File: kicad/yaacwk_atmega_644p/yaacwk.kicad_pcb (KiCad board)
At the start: 2 copper layers, 110 x 78 mm, 61 parts, among them IC1 ATMEGA644P-P, IC2 TLP627-2, J1 EXT_PWR, J2 AUDIO_IN, J3 TX_PTT, J4 TX_KEY, J5 PADDLES, J6 TTL_SERIAL, SW1 SW_PUSH, SW2 SW_PUSH, SW3 SW_PUSH, SW4 SW_PUSH, SW5 SW_PUSH, SW6 SW_PUSH, U1 LM7805, Y1 Crystal 16 Mhz

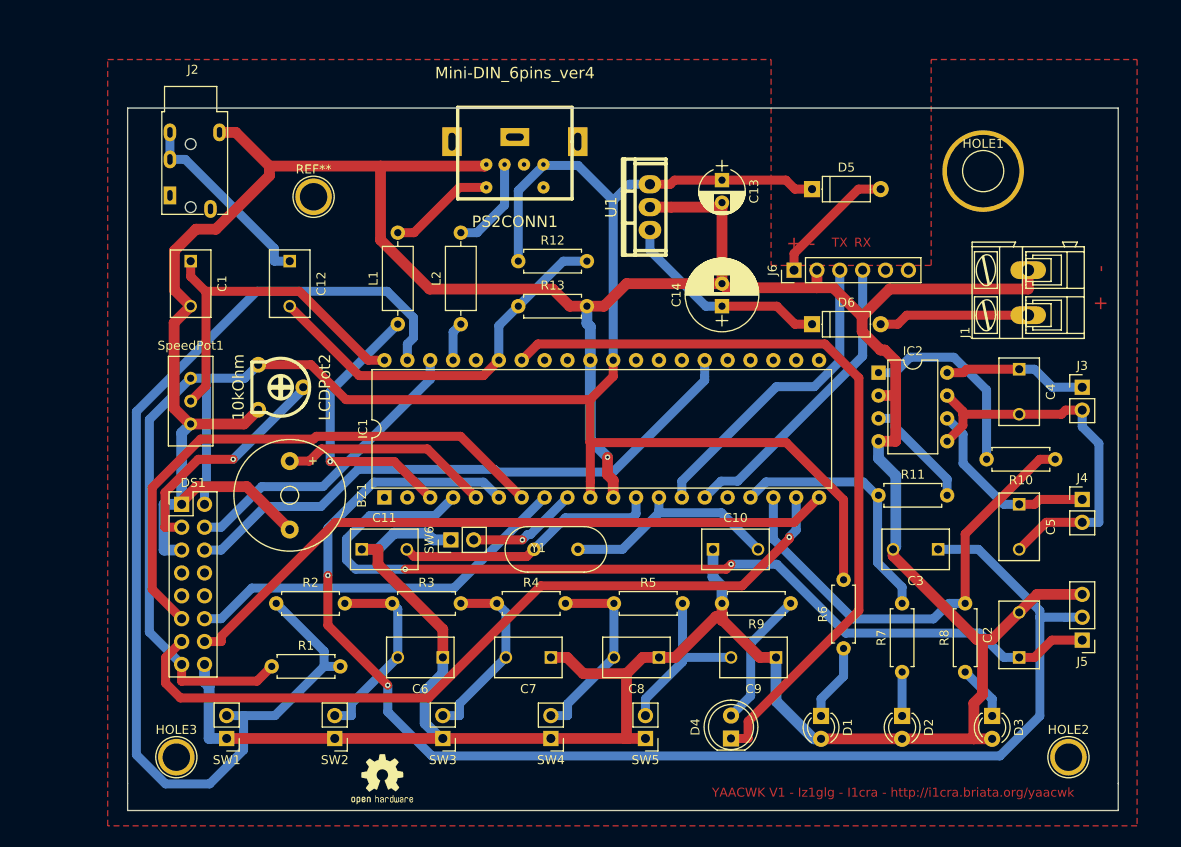
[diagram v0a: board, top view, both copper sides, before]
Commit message: yaacwk pcb v1.1_RC updated eechema
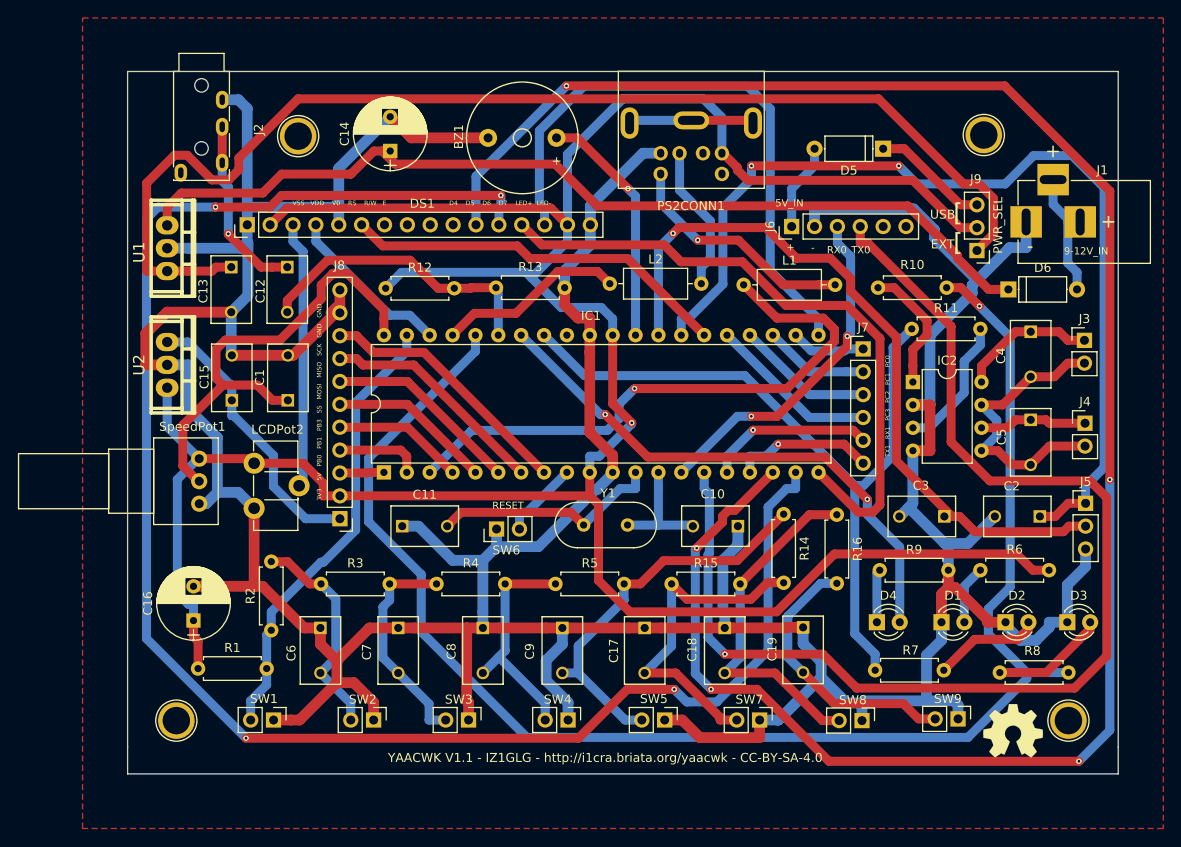
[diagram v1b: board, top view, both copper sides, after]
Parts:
- removed G***: LOGO, OPENHARDWARE:OSHWLOGO0.3IN
- added C15: 220nF, Capacitors_ThroughHole:C_Disc_D7.5_P5, F.Cu at (111.6, 92.5)
- added C16: 330uF, Capacitors_THT:CP_Radial_D8.0mm_P3.80mm, F.Cu at (107.3, 116.9)
- added C17: 100nF, Capacitors_ThroughHole:C_Disc_D7.5_P5, F.Cu at (157.4, 117.7)
- added C18: 100nF, Capacitors_ThroughHole:C_Disc_D7.5_P5, F.Cu at (166.3, 117.7)
- added C19: 100nF, Capacitors_ThroughHole:C_Disc_D7.5_P5, F.Cu at (175.0, 117.7)
- added J7: HEADER_6, Pin_Headers:Pin_Header_Straight_1x06_Pitch2.54mm, F.Cu at (181.7, 86.7)
- added J8: HEADER_11, Pin_Headers:Pin_Header_Straight_1x11_Pitch2.54mm, F.Cu at (123.6, 105.6)
- added J9: PWR_SEL, Pin_Headers:Pin_Header_Straight_1x03_Pitch2.54mm, F.Cu at (194.3, 75.8)
- added R14: 1kOhm, Resistors_THT:R_Axial_DIN0207_L6.3mm_D2.5mm_P7.62mm_Horizontal, F.Cu at (172.8, 105.1)
- added R15: 1kOhm, Resistors_THT:R_Axial_DIN0207_L6.3mm_D2.5mm_P7.62mm_Horizontal, F.Cu at (160.4, 112.8)
- added R16: 1kOhm, Resistors_THT:R_Axial_DIN0207_L6.3mm_D2.5mm_P7.62mm_Horizontal, F.Cu at (178.8, 105.2)
- added REF***: OSHW-Symbol_6.7x6mm_SilkScreen, Symbols:OSHW-Symbol_6.7x6mm_SilkScreen, F.Cu at (198.3, 129.2)
- added SW7: SW_PUSH, Pin_Headers:Pin_Header_Straight_1x02_Pitch2.54mm, F.Cu at (170.2, 128.0)
- added SW8: SW_PUSH, Pin_Headers:Pin_Header_Straight_1x02_Pitch2.54mm, F.Cu at (181.5, 128.0)
- added SW9: SW_PUSH, Pin_Headers:Pin_Header_Straight_1x02_Pitch2.54mm, F.Cu at (192.2, 127.8)
- added U2: LM2937, mojes-kicad-footprints:78XX, F.Cu at (104.4, 88.5)
- C13: value 50mF -> 220nF; footprint Capacitors_THT:CP_Radial_D5.0mm_P2.50mm -> Capacitors_ThroughHole:C_Disc_D7.5_P5
- C14: value 350mF -> 330uF; footprint Capacitors_THT:CP_Radial_D8.0mm_P2.50mm -> Capacitors_THT:CP_Radial_D8.0mm_P3.80mm
- D4: footprint LEDs:LED_D5.0mm -> LEDs:LED_D3.0mm
- DS1: footprint Pin_Headers:Pin_Header_Straight_2x08_Pitch2.54mm -> Pin_Headers:Pin_Header_Straight_1x16_Pitch2.54mm
- HOLE1: footprint Connectors:1pin -> Connect:1pin
- J1: footprint Connect:AK300-2 -> Connectors:BARREL_JACK
- J2: footprint custom_kicad_footprints:PJ320E_3.5mm_4_conductors_audio_plug -> PJ320A:PJ320A_3.5mm_4_conductors_audio_plug
- LCDPot2: footprint w_pth_resistors:trimmer_piher_pt6xv -> Potentiometers:Potentiometer_Trimmer_ACP_CA9h5_Vertical_Px5.0mm_Py5.0mm
- PS2CONN1: footprint mini_din6:Mini_din6 -> mini_din6New:Mini_din6
- R6, R7, R8: value 1kOhm -> 470 Ohm
- SpeedPot1: footprint Potentiometers:Potentiometer_Trimmer_Suntan_TSR-3386C_Vertical -> Potentiometers:Potentiometer_Alps_RK097_Single_Vertical
- Y1: value Crystal 16 Mhz -> Crystal 16 MHz
- moved C13 55.3 mm to (111.5, 77.7)
- moved U1 53.8 mm to (104.4, 75.6), turned to 270 degrees
- moved BZ1 47.4 mm to (143.8, 63.3), turned to 180 degrees
- moved C14 40.7 mm to (129.2, 64.8)
- moved L1 38.6 mm to (168.4, 79.6), turned to 0 degrees
- moved DS1 31.9 mm to (113.3, 73.0), turned to 90 degrees
- moved C9 24.0 mm to (148.3, 117.7), turned to 270 degrees
- moved R10 22.5 mm to (190.9, 79.9)
- moved D6 22.1 mm to (197.8, 80.1)
- moved D4 20.7 mm to (183.2, 117.1), turned to 0 degrees
- moved C8 19.8 mm to (139.4, 117.7), turned to 270 degrees
- moved C1 18.9 mm to (117.8, 92.5), turned to 90 degrees
- moved R11 18.8 mm to (187.1, 84.5)
- moved PS2CONN1 18.3 mm to (161.3, 64.5)
- moved R6 17.5 mm to (194.7, 111.3), turned to 0 degrees
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- renumbered REF** to HOLE0
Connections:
- D1 pad 1: Net-(D1-Pad1) -> GND
- D1 pad 2: GND -> Net-(D1-Pad2)
- D2 pad 1: Net-(D2-Pad1) -> GND
- D2 pad 2: GND -> Net-(D2-Pad2)
- D3 pad 1: Net-(D3-Pad1) -> GND
- D3 pad 2: GND -> Net-(D3-Pad2)
- D5 pad 1: Net-(C13-Pad1) -> Net-(D5-Pad1)
- DS1 pad 15: Net-(C13-Pad1) -> Net-(C16-Pad1)
- DS1 pad 2: Net-(C13-Pad1) -> Net-(C16-Pad1)
- IC1 pad 10: Net-(C13-Pad1) -> Net-(C16-Pad1)
- IC1 pad 18: Net-(IC1-Pad18) -> Net-(DS1-Pad11)
- IC1 pad 19: Net-(DS1-Pad13) -> Net-(DS1-Pad12)
- IC1 pad 20: Net-(DS1-Pad14) -> Net-(DS1-Pad13)
- IC1 pad 21: Net-(IC1-Pad21) -> Net-(DS1-Pad14)
- IC1 pad 27: Net-(IC1-Pad27) -> Net-(C2-Pad1)
- IC1 pad 28: Net-(IC1-Pad28) -> Net-(C3-Pad1)
- IC1 pad 29: Net-(IC1-Pad29) -> Net-(BZ1-Pad1)
- IC1 pad 30: Net-(C13-Pad1) -> Net-(C16-Pad1)
- IC1 pad 34: Net-(D4-Pad1) -> Net-(D4-Pad2)
- IC1 pad 4: Net-(C2-Pad1) -> Net-(IC1-Pad4)
- IC1 pad 5: Net-(BZ1-Pad1) -> Net-(IC1-Pad5)
- IC1 pad 6: Net-(C3-Pad1) -> Net-(IC1-Pad6)
- IC1 pad 7: Net-(DS1-Pad11) -> Net-(IC1-Pad7)
- IC1 pad 8: Net-(DS1-Pad12) -> Net-(IC1-Pad8)
- J1 pad 1: Net-(D6-Pad2) -> GND
- J1 pad 2: GND -> Net-(D6-Pad2)
- J2 pad 2: Net-(C12-Pad1) -> GND
- J2 pad 4: Net-(J2-Pad4) -> Net-(C12-Pad1)
- J2 pad 5: GND -> Net-(J2-Pad5)
- LCDPot2 pad 1: Net-(C13-Pad1) -> Net-(C16-Pad1)
- PS2CONN1 pad 4: Net-(C13-Pad1) -> Net-(C16-Pad1)
- R1 pad 1: Net-(C13-Pad1) -> Net-(C16-Pad1)
- R10 pad 1: Net-(IC1-Pad18) -> Net-(IC1-Pad36)
- R11 pad 1: Net-(IC1-Pad17) -> Net-(IC1-Pad33)
- R12 pad 1: Net-(C13-Pad1) -> Net-(C16-Pad1)
- R6 pad 1: Net-(D1-Pad1) -> Net-(D1-Pad2)
- R6 pad 2: Net-(C13-Pad1) -> Net-(C16-Pad1)
- R7 pad 1: Net-(D2-Pad1) -> Net-(D2-Pad2)
- R7 pad 2: Net-(IC1-Pad17) -> Net-(IC1-Pad33)
- R8 pad 1: Net-(D3-Pad1) -> Net-(D3-Pad2)
- R8 pad 2: Net-(IC1-Pad18) -> Net-(IC1-Pad36)
- R9 pad 1: Net-(D4-Pad2) -> Net-(D4-Pad1)
- SpeedPot1 pad 1: Net-(C13-Pad1) -> Net-(C16-Pad1)
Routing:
- net Net-(C16-Pad1): track 0.00 -> 303.1 mm, vias 0 -> 1
- net Net-(IC1-Pad36): track 0.00 -> 169.7 mm, vias 0 -> 1
- net Net-(DS1-Pad11): track 62.1 -> 222.5 mm, vias 0 -> 5
- net Net-(DS1-Pad12): track 43.3 -> 190.9 mm, vias 0 -> 4
- net Net-(IC1-Pad15): track 33.6 -> 132.7 mm, vias 0 -> 1
- net Net-(C13-Pad1): track 226.7 -> 131.4 mm
- net Net-(IC1-Pad33): track 0.00 -> 83.4 mm
- net Net-(C14-Pad1): track 23.7 -> 105.4 mm
- net Net-(D4-Pad1): track 86.8 -> 5.91 mm
- net Net-(IC1-Pad39): track 123.3 -> 50.1 mm
- net Net-(C3-Pad1): track 151.7 -> 82.0 mm, vias 2 -> 1
- net Net-(IC1-Pad18): track 51.4 -> 0.00 mm
- net Net-(D4-Pad2): track 15.2 -> 61.1 mm, vias 0 -> 2
- net GND: track 482.7 -> 527.5 mm, vias 1 -> 0
- net Net-(C18-Pad2): track 0.00 -> 39.4 mm
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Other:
- board text added: "3V3 5V PB0 PB1 PB3 SS MOSI MISO SCK GND GND"
- board text added: "5V_IN"
- board text added: "9-12V_IN"
- board text added: "EXT"
- board text added: "PWR_SEL"
- board text added: "RESET"
- board text added: "RX0"
- board text added: "TX0"
- board text added: "TX1 RX1 PC3 PC2 PC1 PC0"
- board text added: "USB"
- board text added: "VSS VDD V0 RS R/W E D4 D5 D6 D7 LED+ LED-"
- board text added: "YAACWK V1.1 - IZ1GLG - http://i1cra.briata.org/yaacwk - CC-BY-SA-4.0"
- board text added: "["
- board text removed: "+ -"
- board text removed: "RX"
- board text removed: "TX"
- board text removed: "YAACWK V1 - Iz1glg - I1cra - http://i1cra.briata.org/yaacwk"
